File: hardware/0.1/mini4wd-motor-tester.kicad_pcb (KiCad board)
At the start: 2 copper layers, 100 x 48 mm, 103 parts, among them J1 USB_C_Receptacle_USB2.0_16P, J2 JST SH, J3 JST SH, J4 JST XH, M1 Motor_DC, Q2 AO3401A, Q3 2N7002, SW1 RA, SW2 RA, SW3 EC11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

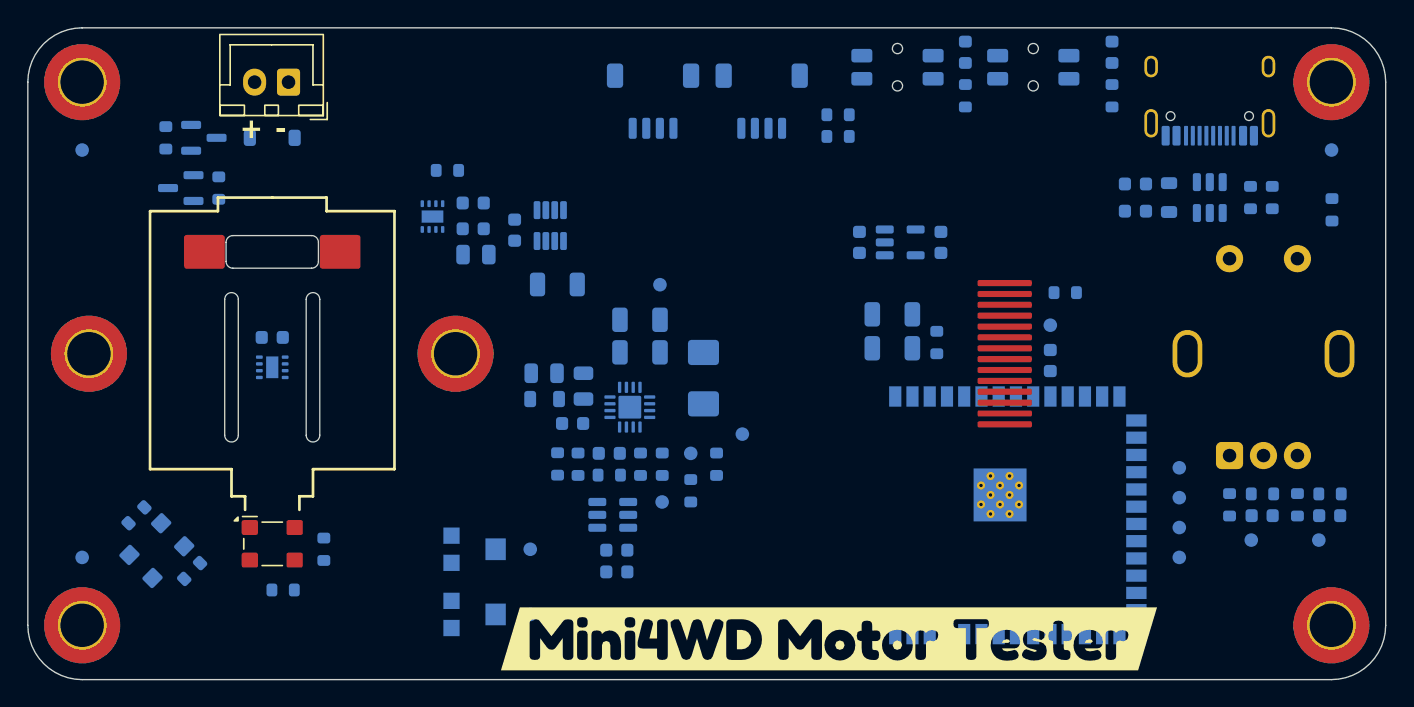
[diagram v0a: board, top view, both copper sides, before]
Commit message: change opto, move motor lower
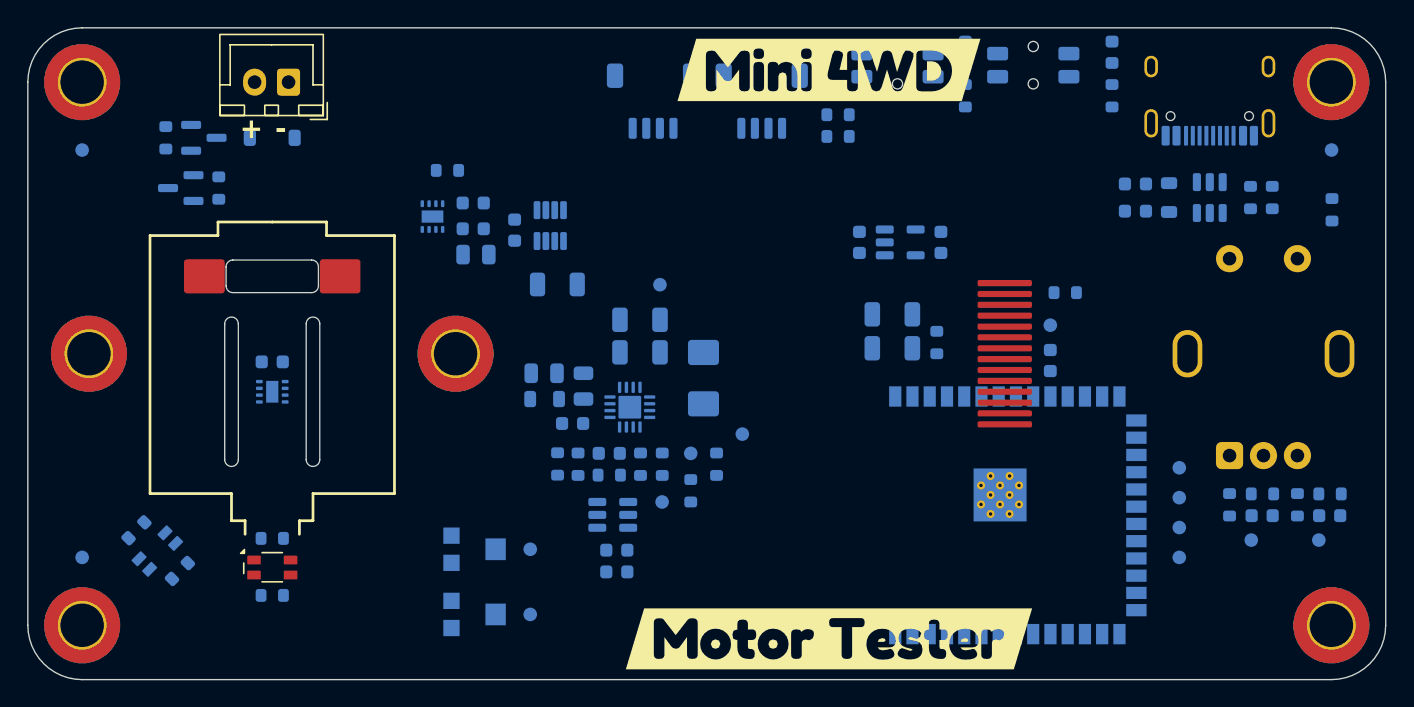
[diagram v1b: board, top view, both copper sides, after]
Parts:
- removed kibuzzard-697A0689: G***, kibuzzard-697A0689
- added kibuzzard-697CCA76: G***, kibuzzard-697CCA76, F.Cu at (125.0, 79.1)
- added kibuzzard-697CCA92: G***, kibuzzard-697CCA92, F.Cu at (125.0, 121.0)
- R22, R26: value 2K2 -> 1K
- U10, U8: value GP2S700HCP -> GP2S60B; footprint josh-passives-smt:Sharp_GP2S700HCP -> josh-passives-smt:Sharp_GP2S60B
- moved R17 5.10 mm to (84.0, 117.8), turned to 0 degrees
- moved R22 3.88 mm to (84.0, 113.6)
- moved C22 1.80 mm to (84.0, 100.6)
- moved M1 1.80 mm to (84.0, 98.3)
- moved U8 1.80 mm to (84.0, 115.8)
- moved U9 1.80 mm to (84.0, 102.8)
- moved R25 1.10 mm to (74.0, 113.0)
- moved R26 0.90 mm to (77.2, 116.0)
- moved SW1 0.15 mm to (130.0, 78.8)
- moved SW2 0.15 mm to (140.0, 78.8)
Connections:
- U10 pad 1: GND -> Net-(R26-Pad2)
- U10 pad 2: Net-(R26-Pad2) -> GND
- U8 pad 1: GND -> Net-(R22-Pad2)
- U8 pad 2: Net-(R22-Pad2) -> GND
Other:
- outline, holes or cut-outs redrawn

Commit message: board passing erc and drc
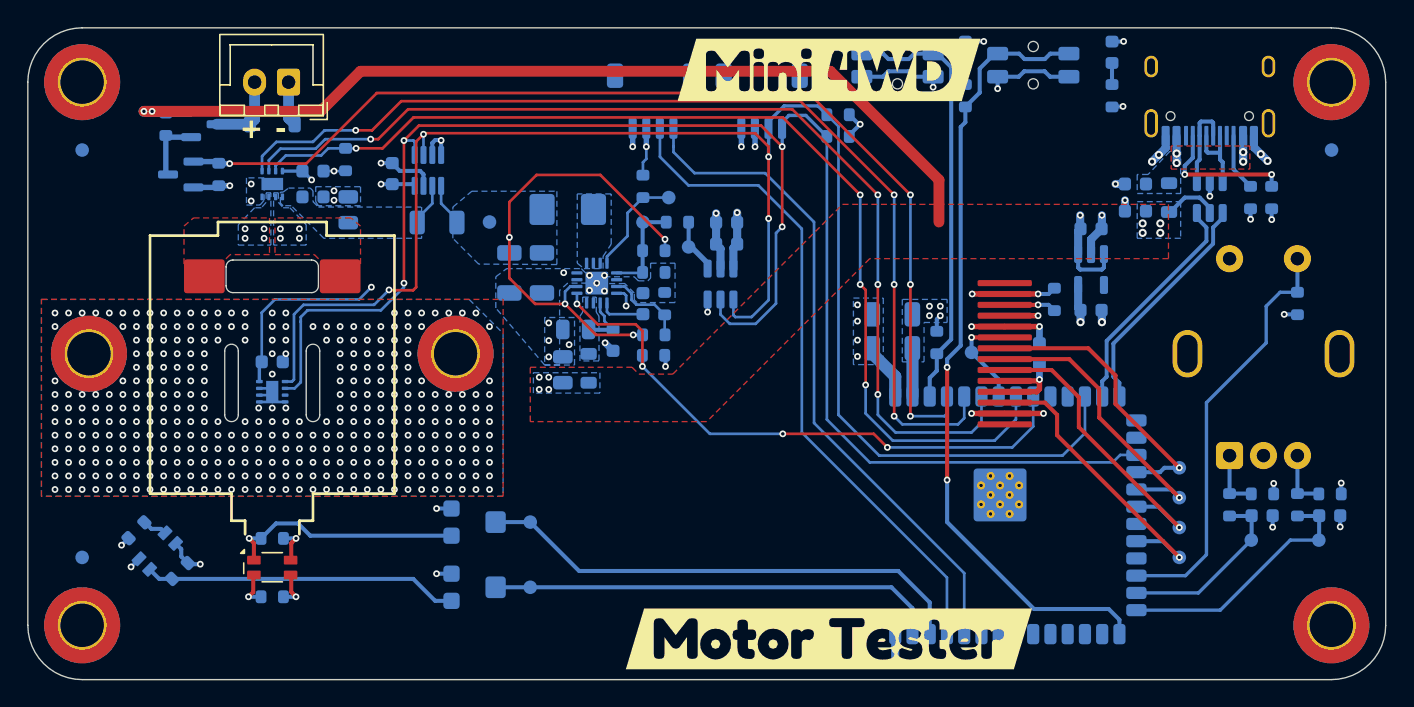
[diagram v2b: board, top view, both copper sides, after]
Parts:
- moved C12 27.0 mm to (117.5, 90.3)
- moved C11 23.9 mm to (117.5, 91.9)
- moved R6 21.2 mm to (111.3, 87.7), turned to -90 degrees
- moved R9 19.8 mm to (113.8, 90.3), turned to 0 degrees
- moved TP2 18.9 mm to (114.7, 92.1), turned to 0 degrees
- moved U4 18.8 mm to (117.0, 94.9), turned to -90 degrees
- moved TP13 18.2 mm to (113.2, 88.5), turned to 90 degrees
- moved TP1 17.4 mm to (111.3, 90.3), turned to 90 degrees
- moved C7 17.1 mm to (144.3, 90.8), turned to 180 degrees
- moved L1 15.9 mm to (105.8, 89.4), turned to 180 degrees
- moved R7 15.7 mm to (112.1, 92.4), turned to 180 degrees
- moved U3 14.2 mm to (144.3, 93.8), turned to -90 degrees
- moved R8 14.2 mm to (112.1, 94.0), turned to 0 degrees
- moved TP3 13.4 mm to (100.0, 90.3)
- moved R3 13.3 mm to (112.9, 96.3), turned to 90 degrees
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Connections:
- U5 pad 10: /MOTOR_IN1 -> unconnected-(U5-IO17-Pad10)
- U5 pad 11: /MOTOR_IN2 -> unconnected-(U5-IO18-Pad11)
- U5 pad 23: /MOTOR_EN -> unconnected-(U5-IO21-Pad23)
- U5 pad 24: unconnected-(U5-IO47-Pad24) -> /ENCODER_SW
- U5 pad 25: unconnected-(U5-IO48-Pad25) -> /ENCODER_A
- U5 pad 26: unconnected-(U5-IO45-Pad26) -> /ENCODER_B
- U5 pad 38: /AUX_5V_EN -> /MOTOR_OUT
- U5 pad 4: /ENCODER_SW -> /AUX_5V_EN
- U5 pad 5: /ENCODER_A -> /MOTOR_IN2
- U5 pad 6: /ENCODER_B -> /MOTOR_IN1
- U5 pad 8: /MOTOR_OUT -> /MOTOR_EN
- U7 pad 2: Net-(M1-+) -> Net-(M1--)
- U7 pad 3: Net-(M1--) -> Net-(M1-+)
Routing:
- net /I2C_SCL: track 0.00 -> 125.2 mm, vias 0 -> 4
- net /I2C_SDA: track 0.00 -> 122.7 mm, vias 0 -> 4
- net GND: track 0.00 -> 90.4 mm, vias 0 -> 413
- net +5V: track 0.00 -> 80.7 mm, vias 0 -> 11
- net /AUX_5V_EN: track 0.00 -> 78.5 mm, vias 0 -> 4
- net /MOTOR_EN: track 0.00 -> 77.8 mm, vias 0 -> 4
- net /MOTOR_IN1: track 0.00 -> 76.4 mm, vias 0 -> 4
- net /MOTOR_IN2: track 0.00 -> 75.7 mm, vias 0 -> 4
- net /ESP0/STAT: track 0.00 -> 58.5 mm, vias 0 -> 2
- net +3V3: track 0.00 -> 56.5 mm, vias 0 -> 20
- net /RXD: track 0.00 -> 49.2 mm
- net /TXD: track 0.00 -> 49.0 mm
- net /REG_EN: track 0.00 -> 43.9 mm, vias 0 -> 4
- net +VMOT: track 0.00 -> 37.2 mm, vias 0 -> 4
- net /MOTOR_OUT: track 0.00 -> 36.8 mm
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- added copper zone on B.Cu, net +3V3
- added copper zone on In2.Cu, net +3V3
- added copper zone on B.Cu, net +5V
- added copper zone on F.Cu, net +5V
- added copper zone on B.Cu, net +VMOT
- added copper zone on B.Cu, net GND
- added copper zone on F.Cu, net GND
- added copper zone on In1.Cu, net GND
- added copper zone on In2.Cu, net GND
- added copper zone on B.Cu, net Net-(C5-Pad2)
- added copper zone on F.Cu, net Net-(C5-Pad2)
- added copper zone on B.Cu, net Net-(L1-Pad1)
- added copper zone on B.Cu, net Net-(M1-+)
- added copper zone on F.Cu, net Net-(M1-+)
- added copper zone on B.Cu, net Net-(M1--)
- added copper zone on F.Cu, net Net-(M1--)
- added copper zone on B.Cu, net Net-(U1-AVIN)
- added copper zone on B.Cu, net Net-(U6-IN-)
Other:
- outline, holes or cut-outs redrawn
- copper layers 2 -> 4
- rule pad_to_mask_clearance: 0 -> 0.05
- board text added: "MINI4WD MOTOR TESTER REVISION 0.1"
- board text removed: "MINI4WD MOTOR TESTER REVISION 1.0"

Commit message: off to fab
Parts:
- added F1: 2A, Fuse:Fuse_1206_3216Metric, B.Cu at (149.7, 88.9)
- added TP14: TP, TestPoint:TestPoint_Pad_D1.0mm, B.Cu at (143.5, 85.3)
- C12, C5, C6: value 1u -> 10u; footprint Capacitor_SMD:C_0603_1608Metric -> Capacitor_SMD:C_0805_2012Metric
- moved C10 12.0 mm to (141.0, 85.3), turned to 0 degrees
- moved U3 6.60 mm to (140.8, 88.2), turned to 90 degrees
- moved FB2 4.98 mm to (146.5, 92.0), turned to 0 degrees
- moved C7 3.52 mm to (140.8, 91.2), turned to 0 degrees
- moved R24 2.40 mm to (139.2, 96.0)
- moved C6 2.07 mm to (145.5, 89.4), turned to 90 degrees
- moved C5 1.90 mm to (147.5, 89.4), turned to 90 degrees
- moved C12 0.13 mm to (117.5, 90.2), turned to 180 degrees
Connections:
- C12 pad 1: GND -> +3V3
- C12 pad 2: +3V3 -> GND
- C5 pad 1: GND -> Net-(C5-Pad1)
- C5 pad 2: Net-(C5-Pad2) -> GND
- C6 pad 1: GND -> +5V
- C6 pad 2: +5V -> GND
- FB2 pad 2: Net-(C5-Pad2) -> Net-(C5-Pad1)
- J1 pad A4: Net-(C5-Pad2) -> Net-(F1-Pad1)
- J1 pad A9: Net-(C5-Pad2) -> Net-(F1-Pad1)
- J1 pad B4: Net-(C5-Pad2) -> Net-(F1-Pad1)
- J1 pad B9: Net-(C5-Pad2) -> Net-(F1-Pad1)
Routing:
- net +5V: track 80.7 -> 86.0 mm
- net Net-(F1-Pad1): track 0.00 -> 3.90 mm, vias 0 -> 4
- net Net-(C5-Pad2): track 3.90 -> 0.00 mm, vias 4 -> 0
- net +3V3: track 56.5 -> 57.6 mm
- net GND: track 90.4 -> 90.5 mm, vias 413 -> 419
- added copper zone on B.Cu, net Net-(C5-Pad1)
- added copper zone on B.Cu, net Net-(F1-Pad1)
- added copper zone on F.Cu, net Net-(F1-Pad1)
- removed copper zone on B.Cu, net Net-(C5-Pad2)
- removed copper zone on F.Cu, net Net-(C5-Pad2)
